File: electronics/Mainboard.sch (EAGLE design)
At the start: 225 parts, among them J1 JST_PH_B3B-PH-K-S(LF)(SN), J10 JST_PH_B3B-PH-K-S(LF)(SN), J11 JST_PH_B3B-PH-K-S(LF)(SN), J12 JST_PH_B3B-PH-K-S(LF)(SN), J13 JST_PH_B3B-PH-K-S(LF)(SN), J14 JST_PH_B3B-PH-K-S(LF)(SN), J15 JST_PH_B3B-PH-K-S(LF)(SN), J16 JST_PH_B3B-PH-K-S(LF)(SN), J17 JST_PH_B3B-PH-K-S(LF)(SN), J18 JST_PH_B3B-PH-K-S(LF)(SN), J19 JST_PH_B3B-PH-K-S(LF)(SN), J2 JST_PH_B3B-PH-K-S(LF)(SN), J20 JST_PH_B3B-PH-K-S(LF)(SN), J21 JST_PH_B3B-PH-K-S(LF)(SN), J22 JST_PH_B3B-PH-K-S(LF)(SN), J23 JST_PH_B3B-PH-K-S(LF)(SN), J24 JST_PH_B3B-PH-K-S(LF)(SN), J25 JST_PH_B3B-PH-K-S(LF)(SN), J26 JST_PH_B3B-PH-K-S(LF)(SN), J27 JST_PH_B3B-PH-K-S(LF)(SN), J28 JST_PH_B3B-PH-K-S(LF)(SN), J29 JST_PH_B3B-PH-K-S(LF)(SN), J3 JST_PH_B3B-PH-K-S(LF)(SN), J30 JST_PH_B3B-PH-K-S(LF)(SN), J31 JST_PH_B3B-PH-K-S(LF)(SN), J32 JST_PH_B3B-PH-K-S(LF)(SN), J33 B4B-PH-K-S(LF)(SN), J34 B4B-PH-K-S(LF)(SN), J35 B4B-PH-K-S(LF)(SN), J36 B4B-PH-K-S(LF)(SN), J37 B4B-PH-K-S(LF)(SN), J38 B4B-PH-K-S(LF)(SN), J39 B4B-PH-K-S(LF)(SN), J4 JST_PH_B3B-PH-K-S(LF)(SN), J40 B4B-PH-K-S(LF)(SN), J41 B4B-PH-K-S(LF)(SN), J42 B4B-PH-K-S(LF)(SN), J43 B4B-PH-K-S(LF)(SN), J44 B4B-PH-K-S(LF)(SN), J45 B4B-PH-K-S(LF)(SN), J46 B4B-PH-K-S(LF)(SN), J47 B4B-PH-K-S(LF)(SN), J48 B4B-PH-K-S(LF)(SN), J49 B4B-PH-K-S(LF)(SN), J5 JST_PH_B3B-PH-K-S(LF)(SN), J50 B4B-PH-K-S(LF)(SN), J51 B4B-PH-K-S(LF)(SN), J52 B4B-PH-K-S(LF)(SN), J53 B4B-PH-K-S(LF)(SN), J54 B4B-PH-K-S(LF)(SN), J55 B4B-PH-K-S(LF)(SN), J56 B4B-PH-K-S(LF)(SN), J57 B4B-PH-K-S(LF)(SN), J58 B4B-PH-K-S(LF)(SN), J59 B4B-PH-K-S(LF)(SN), J6 JST_PH_B3B-PH-K-S(LF)(SN), J60 B4B-PH-K-S(LF)(SN), J61 B4B-PH-K-S(LF)(SN), J62 B4B-PH-K-S(LF)(SN), J63 B4B-PH-K-S(LF)(SN), J64 B4B-PH-K-S(LF)(SN), J7 JST_PH_B3B-PH-K-S(LF)(SN), J8 JST_PH_B3B-PH-K-S(LF)(SN), J9 JST_PH_B3B-PH-K-S(LF)(SN), U1 AMP-5103309-7-34PIN_5103309-7, U15 AD5360BSTZ, U16 ADR425ARZ, U18 AD7730BRUZ, U19 AD5360BSTZ, U2 AMP-5103309-7-34PIN_5103309-7, U20 ADR425ARZ, U21 AD7730BRUZ, U22 STM32F103RCT6, U23 AD7730BRUZ, U24 AD7730BRUZ, U25 AD7730BRUZ, U26 AD7730BRUZ, U27 AD7730BRUZ, U28 AD7730BRUZ, U38 AD7730BRUZ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

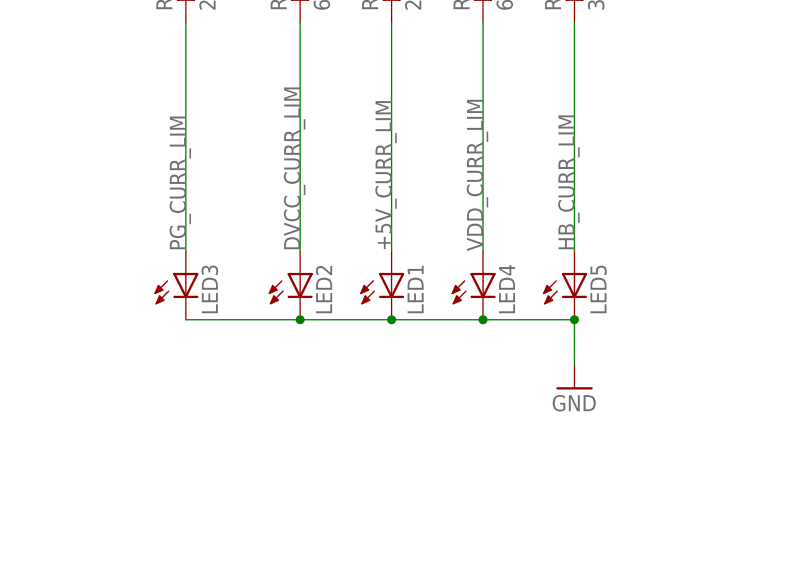
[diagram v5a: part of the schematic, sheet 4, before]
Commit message: switched to smd leds
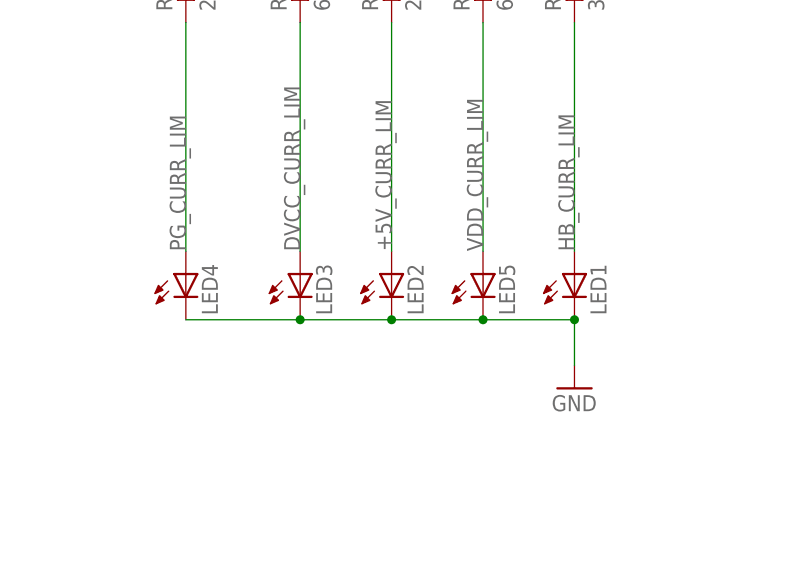
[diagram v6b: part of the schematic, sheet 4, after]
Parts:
- LED1, LED2, LED3, LED4, LED5: value TLLG4400 -> (none); device led:TLLG4400 -> led:LEDCHIP-LED0603
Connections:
- net +5V_CURR_LIM: now also LED2.A; no longer LED1.A
- net DVCC_CURR_LIM: now also LED3.A; no longer LED2.A
- net HB_CURR_LIM: now also LED1.A; no longer LED5.A
- net PG_CURR_LIM: now also LED4.A; no longer LED3.A
- net VDD_CURR_LIM: now also LED5.A; no longer LED4.A
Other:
- moved on the sheet: LED1, LED2, LED3, LED4, LED5
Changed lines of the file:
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@@
 <part name="S1" library="1MS1T1B1M2QES-5" deviceset="1MS1T1B1M2QES-5" device="" value=""/>
 <part name="GND135" library="supply1" library_urn="urn:adsk.eagle:library:371" deviceset="GND" device=""/>
-<part name="LED3" library="led" library_urn="urn:adsk.eagle:library:259" deviceset="TLLG4400" device="" package3d_urn="urn:adsk.eagle:package:15797/1" value=""/>
-<part name="LED2" library="led" library_urn="urn:adsk.eagle:library:259" deviceset="TLLG4400" device="" package3d_urn="urn:adsk.eagle:package:15797/1" value=""/>
-<part name="LED1" library="led" library_urn="urn:adsk.eagle:library:259" deviceset="TLLG4400" device="" package3d_urn="urn:adsk.eagle:package:15797/1" value=""/>
-<part name="LED4" library="led" library_urn="urn:adsk.eagle:library:259" deviceset="TLLG4400" device="" package3d_urn="urn:adsk.eagle:package:15797/1" value=""/>
 <part name="GND136" library="supply1" library_urn="urn:adsk.eagle:library:371" deviceset="GND" device=""/>
 <part name="R1" library="resistor" library_urn="urn:adsk.eagle:library:348" deviceset="R-EU_" device="R0805" package3d_urn="urn:adsk.eagle:package:26059/1" value="220"/>
@@
 <part name="X1" library="con-molex" library_urn="urn:adsk.eagle:library:165" deviceset="22-23-2031" device=""/>
 <part name="GND150" library="supply1" library_urn="urn:adsk.eagle:library:371" deviceset="GND" device=""/>
-<part name="LED5" library="led" library_urn="urn:adsk.eagle:library:259" deviceset="TLLG4400" device="" package3d_urn="urn:adsk.eagle:package:15797/1" value=""/>
 <part name="R11" library="resistor" library_urn="urn:adsk.eagle:library:348" deviceset="R-EU_" device="R0805" package3d_urn="urn:adsk.eagle:package:26059/1" value="330"/>
 <part name="C1" library="resistor" library_urn="urn:adsk.eagle:library:348" deviceset="CPOL-EU" device="SMCA" package3d_urn="urn:adsk.eagle:package:25926/1" value="10uF"/>
@@
 <part name="C29" library="resistor" library_urn="urn:adsk.eagle:library:348" deviceset="CPOL-EU" device="SMCA" package3d_urn="urn:adsk.eagle:package:25926/1" value="10uF"/>
 <part name="C30" library="resistor" library_urn="urn:adsk.eagle:library:348" deviceset="CPOL-EU" device="SMCA" package3d_urn="urn:adsk.eagle:package:25926/1" value="10uF"/>
+<part name="LED1" library="led" library_urn="urn:adsk.eagle:library:259" deviceset="LED" device="CHIP-LED0603" package3d_urn="urn:adsk.eagle:package:15819/3"/>
+<part name="LED5" library="led" library_urn="urn:adsk.eagle:library:259" deviceset="LED" device="CHIP-LED0603" package3d_urn="urn:adsk.eagle:package:15819/3"/>
+<part name="LED2" library="led" library_urn="urn:adsk.eagle:library:259" deviceset="LED" device="CHIP-LED0603" package3d_urn="urn:adsk.eagle:package:15819/3"/>
+<part name="LED3" library="led" library_urn="urn:adsk.eagle:library:259" deviceset="LED" device="CHIP-LED0603" package3d_urn="urn:adsk.eagle:package:15819/3"/>
+<part name="LED4" library="led" library_urn="urn:adsk.eagle:library:259" deviceset="LED" device="CHIP-LED0603" package3d_urn="urn:adsk.eagle:package:15819/3"/>
 </parts>
 <sheets>
@@
 <instance part="S1" gate="G$1" x="403.86" y="259.08"/>
 <instance part="GND135" gate="1" x="431.8" y="254"/>
-<instance part="LED3" gate="G$1" x="312.42" y="231.14"/>
-<instance part="LED2" gate="G$1" x="325.12" y="231.14"/>
-<instance part="LED1" gate="G$1" x="335.28" y="231.14"/>
-<instance part="LED4" gate="G$1" x="345.44" y="231.14"/>
 <instance part="GND136" gate="1" x="355.6" y="218.44"/>
 <instance part="R1" gate="G$1" x="312.42" y="264.16" rot="R90"/>
@@
 <instance part="X1" gate="-3" x="116.84" y="259.08"/>
 <instance part="GND150" gate="1" x="104.14" y="254"/>
-<instance part="LED5" gate="G$1" x="355.6" y="231.14"/>
 <instance part="R11" gate="G$1" x="355.6" y="264.16" rot="R90"/>
+<instance part="LED1" gate="G$1" x="355.6" y="231.14"/>
+<instance part="LED5" gate="G$1" x="345.44" y="231.14"/>
+<instance part="LED2" gate="G$1" x="335.28" y="231.14"/>
+<instance part="LED3" gate="G$1" x="325.12" y="231.14"/>
+<instance part="LED4" gate="G$1" x="312.42" y="231.14"/>
 </instances>
 <busses>
@@
 </segment>
 <segment>
-<pinref part="LED3" gate="G$1" pin="C"/>
-<pinref part="LED2" gate="G$1" pin="C"/>
 <wire x1="312.42" y1="226.06" x2="325.12" y2="226.06" width="0.1524" layer="91"/>
-<pinref part="LED1" gate="G$1" pin="C"/>
 <wire x1="325.12" y1="226.06" x2="335.28" y2="226.06" width="0.1524" layer="91"/>
-<junction x="325.12" y="226.06"/>
-<pinref part="LED4" gate="G$1" pin="C"/>
 <wire x1="335.28" y1="226.06" x2="345.44" y2="226.06" width="0.1524" layer="91"/>
-<junction x="335.28" y="226.06"/>
 <wire x1="345.44" y1="226.06" x2="355.6" y2="226.06" width="0.1524" layer="91"/>
-<junction x="345.44" y="226.06"/>
 <wire x1="355.6" y1="226.06" x2="355.6" y2="220.98" width="0.1524" layer="91"/>
 <pinref part="GND136" gate="1" pin="GND"/>
-<pinref part="LED5" gate="G$1" pin="C"/>
+<pinref part="LED1" gate="G$1" pin="C"/>
 <junction x="355.6" y="226.06"/>
+<pinref part="LED5" gate="G$1" pin="C"/>
+<junction x="345.44" y="226.06"/>
+<pinref part="LED2" gate="G$1" pin="C"/>
+<junction x="335.28" y="226.06"/>
+<pinref part="LED3" gate="G$1" pin="C"/>
+<junction x="325.12" y="226.06"/>
+<pinref part="LED4" gate="G$1" pin="C"/>
 </segment>
 <segment>
@@
 <net name="PG_CURR_LIM" class="0">
 <segment>
-<pinref part="LED3" gate="G$1" pin="A"/>
 <pinref part="R1" gate="G$1" pin="1"/>
 <wire x1="312.42" y1="233.68" x2="312.42" y2="259.08" width="0.1524" layer="91"/>
 <label x="312.42" y="233.68" size="1.778" layer="95" rot="R90"/>
+<pinref part="LED4" gate="G$1" pin="A"/>
 </segment>
 </net>
 <net name="DVCC_CURR_LIM" class="0">
 <segment>
-<pinref part="LED2" gate="G$1" pin="A"/>
 <pinref part="R3" gate="G$1" pin="1"/>
 <wire x1="325.12" y1="233.68" x2="325.12" y2="259.08" width="0.1524" layer="91"/>
 <label x="325.12" y="233.68" size="1.778" layer="95" rot="R90"/>
+<pinref part="LED3" gate="G$1" pin="A"/>
 </segment>
 </net>
 <net name="+5V_CURR_LIM" class="0">
 <segment>
-<pinref part="LED1" gate="G$1" pin="A"/>
 <pinref part="R5" gate="G$1" pin="1"/>
 <wire x1="335.28" y1="233.68" x2="335.28" y2="259.08" width="0.1524" layer="91"/>
 <label x="335.28" y="233.68" size="1.778" layer="95" rot="R90"/>
+<pinref part="LED2" gate="G$1" pin="A"/>
 </segment>
 </net>
 <net name="VDD_CURR_LIM" class="0">
 <segment>
-<pinref part="LED4" gate="G$1" pin="A"/>
 <pinref part="R10" gate="G$1" pin="1"/>
 <wire x1="345.44" y1="233.68" x2="345.44" y2="259.08" width="0.1524" layer="91"/>
 <label x="345.44" y="233.68" size="1.778" layer="95" rot="R90"/>
+<pinref part="LED5" gate="G$1" pin="A"/>
 </segment>
 </net>
@@
 <net name="HB_CURR_LIM" class="0">
 <segment>
-<pinref part="LED5" gate="G$1" pin="A"/>
 <pinref part="R11" gate="G$1" pin="1"/>
 <wire x1="355.6" y1="233.68" x2="355.6" y2="259.08" width="0.1524" layer="91"/>
 <label x="355.6" y="233.68" size="1.778" layer="95" rot="R90"/>
+<pinref part="LED1" gate="G$1" pin="A"/>
 </segment>
 </net>

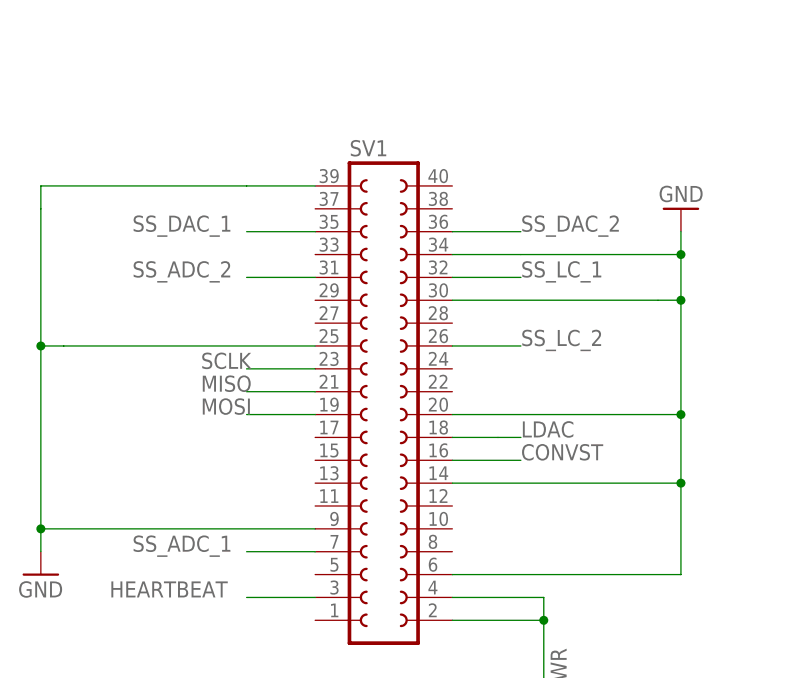
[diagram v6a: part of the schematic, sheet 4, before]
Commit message: re-routed spi bus
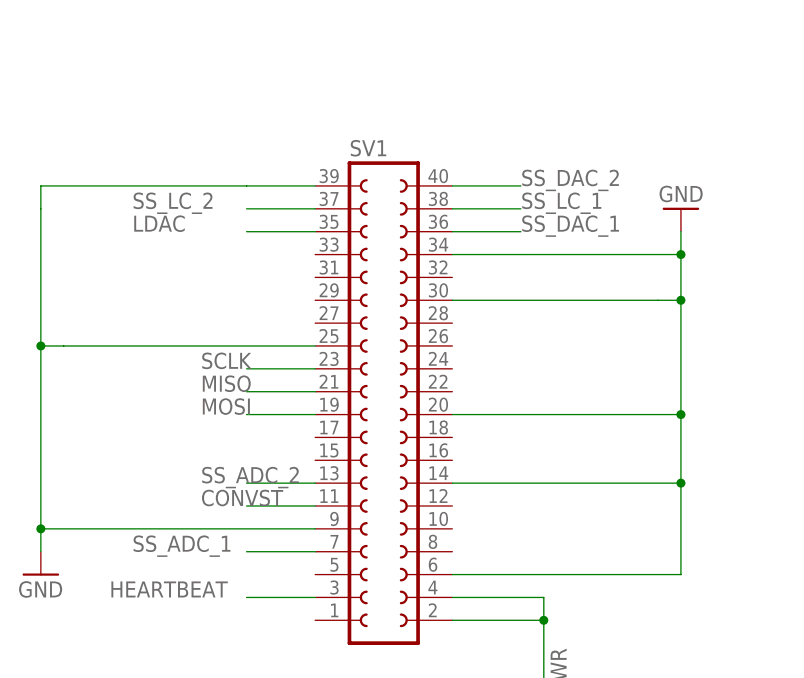
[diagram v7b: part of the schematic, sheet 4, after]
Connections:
- net CONVST: now also SV1.11; no longer SV1.16
- net LDAC: now also SV1.35; no longer SV1.18
- net SS_ADC_2: now also SV1.13; no longer SV1.31
- net SS_DAC_1: now also SV1.36; no longer SV1.35
- net SS_DAC_2: now also SV1.40; no longer SV1.36
- net SS_LC_1: now also SV1.38; no longer SV1.32
- net SS_LC_2: now also SV1.37; no longer SV1.26
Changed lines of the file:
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@@
 <?xml version="1.0" encoding="utf-8"?>
 <!DOCTYPE eagle SYSTEM "eagle.dtd">
-<eagle version="9.0.0">
+<eagle version="9.0.1">
 <drawing>
 <settings>
@@
 </segment>
 </net>
-<net name="LDAC" class="0">
-<segment>
-<pinref part="SV1" gate="G$1" pin="18"/>
-<wire x1="20.32" y1="254" x2="25.4" y2="254" width="0.1524" layer="91"/>
-<wire x1="25.4" y1="254" x2="27.94" y2="254" width="0.1524" layer="91"/>
-<label x="27.94" y="254" size="1.778" layer="95"/>
-</segment>
-</net>
 <net name="CONVST" class="0">
 <segment>
-<pinref part="SV1" gate="G$1" pin="16"/>
-<wire x1="20.32" y1="251.46" x2="27.94" y2="251.46" width="0.1524" layer="91"/>
-<label x="27.94" y="251.46" size="1.778" layer="95"/>
+<pinref part="SV1" gate="G$1" pin="11"/>
+<wire x1="5.08" y1="246.38" x2="-2.54" y2="246.38" width="0.1524" layer="91"/>
+<label x="-7.62" y="246.38" size="1.778" layer="95"/>
 </segment>
 </net>
@@
 <net name="SS_ADC_2" class="0">
 <segment>
-<pinref part="SV1" gate="G$1" pin="31"/>
-<wire x1="5.08" y1="271.78" x2="-2.54" y2="271.78" width="0.1524" layer="91"/>
-<label x="-15.24" y="271.78" size="1.778" layer="95"/>
-</segment>
-</net>
-<net name="SS_DAC_1" class="0">
-<segment>
-<pinref part="SV1" gate="G$1" pin="35"/>
-<wire x1="5.08" y1="276.86" x2="-2.54" y2="276.86" width="0.1524" layer="91"/>
-<label x="-15.24" y="276.86" size="1.778" layer="95"/>
+<pinref part="SV1" gate="G$1" pin="13"/>
+<wire x1="5.08" y1="248.92" x2="-2.54" y2="248.92" width="0.1524" layer="91"/>
+<label x="-7.62" y="248.92" size="1.778" layer="95"/>
 </segment>
 </net>
 <net name="SS_DAC_2" class="0">
 <segment>
-<pinref part="SV1" gate="G$1" pin="36"/>
-<wire x1="20.32" y1="276.86" x2="27.94" y2="276.86" width="0.1524" layer="91"/>
-<label x="27.94" y="276.86" size="1.778" layer="95"/>
+<pinref part="SV1" gate="G$1" pin="40"/>
+<wire x1="20.32" y1="281.94" x2="27.94" y2="281.94" width="0.1524" layer="91"/>
+<label x="27.94" y="281.94" size="1.778" layer="95"/>
 </segment>
 </net>
 <net name="SS_LC_1" class="0">
 <segment>
-<pinref part="SV1" gate="G$1" pin="32"/>
-<wire x1="20.32" y1="271.78" x2="27.94" y2="271.78" width="0.1524" layer="91"/>
-<label x="27.94" y="271.78" size="1.778" layer="95"/>
+<pinref part="SV1" gate="G$1" pin="38"/>
+<wire x1="20.32" y1="279.4" x2="27.94" y2="279.4" width="0.1524" layer="91"/>
+<label x="27.94" y="279.4" size="1.778" layer="95"/>
 </segment>
 </net>
 <net name="SS_LC_2" class="0">
 <segment>
-<pinref part="SV1" gate="G$1" pin="26"/>
-<wire x1="20.32" y1="264.16" x2="27.94" y2="264.16" width="0.1524" layer="91"/>
-<label x="27.94" y="264.16" size="1.778" layer="95"/>
+<pinref part="SV1" gate="G$1" pin="37"/>
+<wire x1="5.08" y1="279.4" x2="-2.54" y2="279.4" width="0.1524" layer="91"/>
+<label x="-15.24" y="279.4" size="1.778" layer="95"/>
 </segment>
 </net>
@@
 </segment>
 </net>
+<net name="LDAC" class="0">
+<segment>
+<pinref part="SV1" gate="G$1" pin="35"/>
+<wire x1="5.08" y1="276.86" x2="-2.54" y2="276.86" width="0.1524" layer="91"/>
+<label x="-15.24" y="276.86" size="1.778" layer="95"/>
+</segment>
+</net>
+<net name="SS_DAC_1" class="0">
+<segment>
+<pinref part="SV1" gate="G$1" pin="36"/>
+<wire x1="20.32" y1="276.86" x2="27.94" y2="276.86" width="0.1524" layer="91"/>
+<label x="27.94" y="276.86" size="1.778" layer="95"/>
+</segment>
+</net>
